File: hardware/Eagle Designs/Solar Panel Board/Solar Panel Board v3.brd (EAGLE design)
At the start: 82.4 x 96.7 mm, 44 parts, among them J1 MOLEX_503763-0291MOLEX_503763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, J2 MOLEX_503763-0491MOLEX_503763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, J3 MOLEX_503763-0291MOLEX_503763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, U1 TMP36GSZ, U2 INA219BIDR

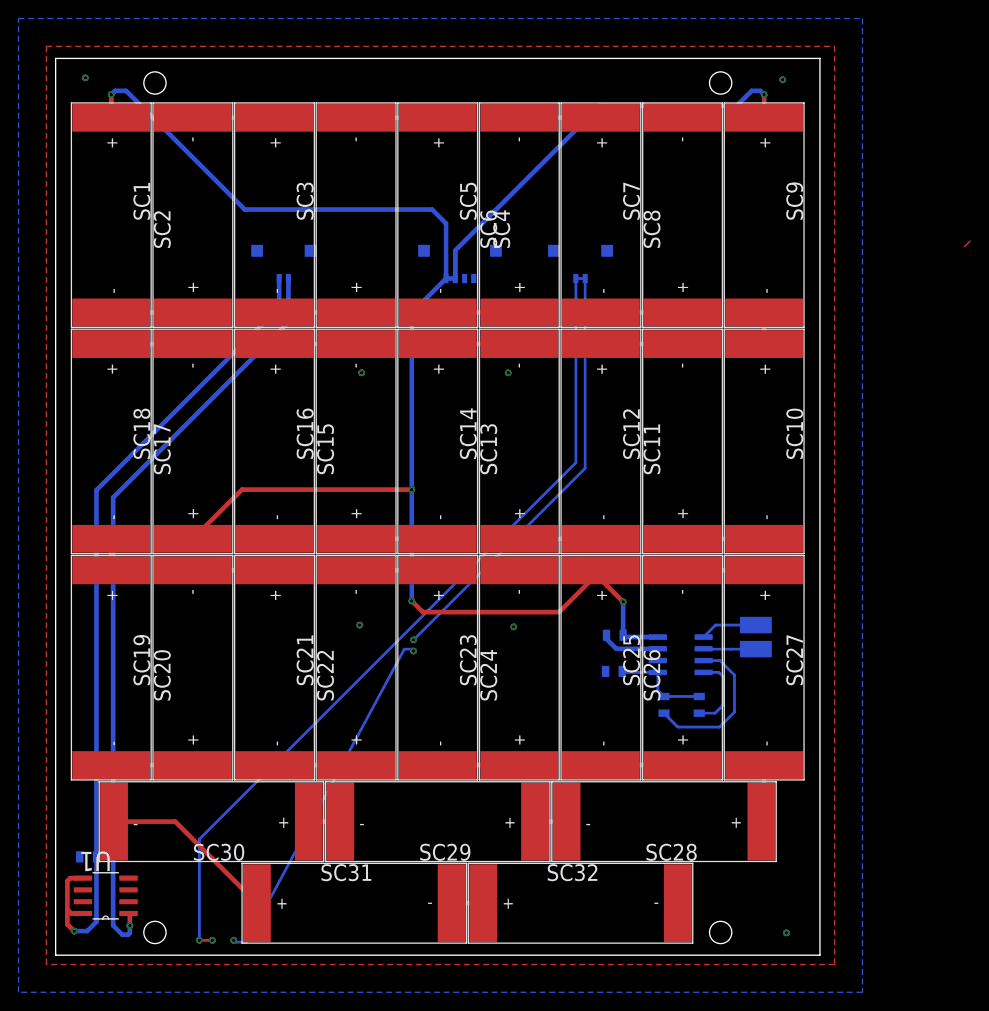
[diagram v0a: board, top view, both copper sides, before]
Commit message: Updated antenna and solar panel boards.
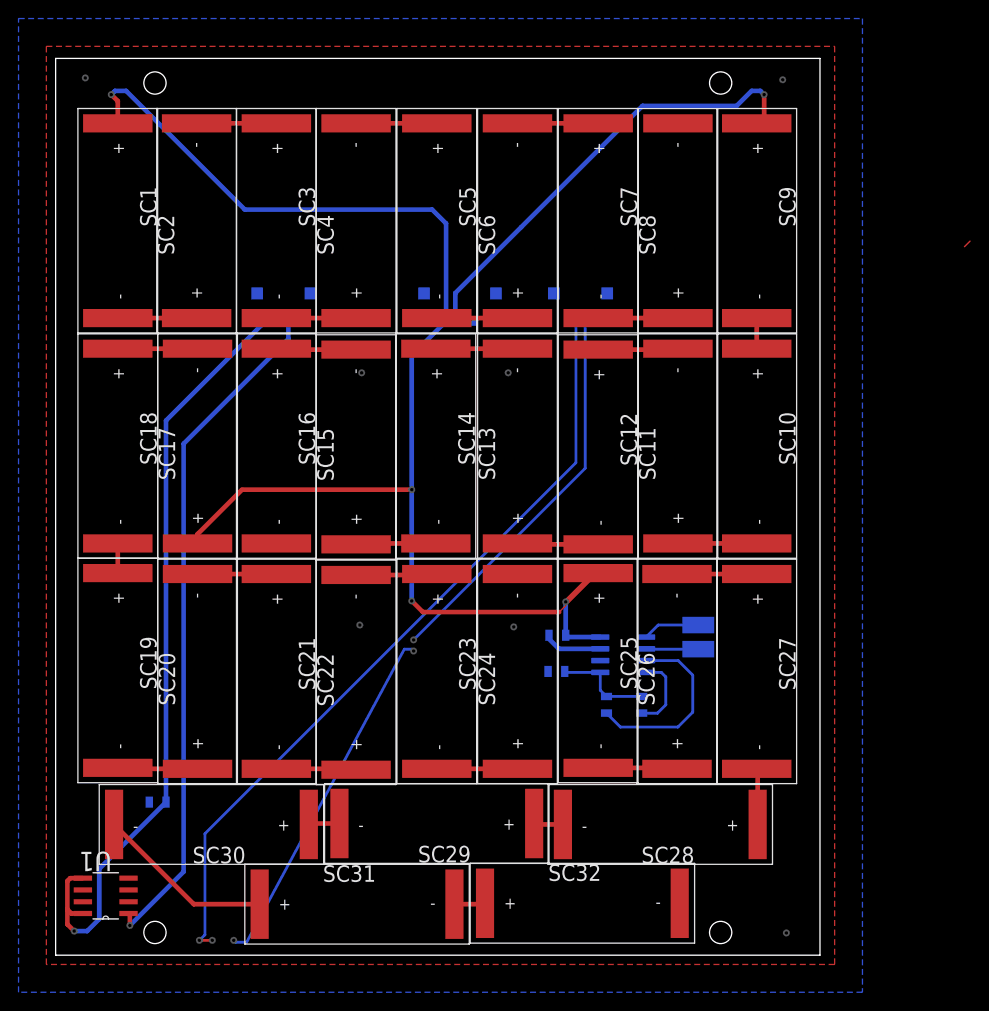
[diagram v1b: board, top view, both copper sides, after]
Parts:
- SC1, SC10, SC11, SC12, SC13, SC14, SC15, SC16, SC17, SC18, SC19, SC2, SC20, SC21, SC22, SC23, SC24, SC25, SC26, SC27, SC28, SC29, SC3, SC30, SC31, SC32, SC4, SC5, SC6, SC7, SC8, SC9: device KXOB25-05X3F:KXOB25-05X3F -> untitled:KXOB25-05X3F
- moved C1 9.54 mm to (11.0, 16.5)
- moved C2 6.20 mm to (54.0, 30.6)
- moved R2 6.20 mm to (63.2, 27.0)
- moved U$1 6.20 mm to (69.3, 33.0)
- moved U$2 6.20 mm to (69.3, 35.6)
- moved U2 6.20 mm to (61.2, 32.4)
- moved R1 6.20 mm to (59.4, 27.0)
- moved R3 6.20 mm to (54.1, 34.5)
- moved J1 4.60 mm to (56.6, 70.8)
- moved J2 4.60 mm to (43.6, 70.8)
- moved J3 4.60 mm to (24.6, 70.8)
- moved SC9 1.00 mm to (75.6, 79.2)
- moved SC10 0.94 mm to (75.6, 54.9)
- moved SC1 0.92 mm to (6.70, 79.2)
- moved SC27 0.89 mm to (75.6, 30.6)
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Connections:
- removed net N$12 (its old number): SC12.-, SC13.+
- removed net N$14 (its old number): SC14.-, SC15.+
- removed net N$19 (its old number): SC20.-, SC21.+
- removed net N$26: SC28.-, SC29.+
- removed net N$28: SC30.-, SC31.+
- removed net N$5 (its old number): SC4.-, SC5.+
- removed net N$7 (its old number): SC6.-, SC7.+
- new net N$15: SC20.-, SC21.+, SC22.-, SC23.+
- new net N$3: SC4.-, SC5.+, SC6.-, SC7.+
- new net N$9: SC12.-, SC13.+, SC14.-, SC15.+
- net N$21: now also SC28.-, SC29.+, SC30.-, SC31.+; no longer SC22.-, SC23.+
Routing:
- net N$28: track 19.0 -> 0.00 mm
- net N$3: track 0.00 -> 18.8 mm
- net N$9: track 0.00 -> 17.4 mm
- net N$15: track 0.00 -> 17.2 mm
- net N$21: track 8.80 -> 22.4 mm
- net N$1: track 22233.0 -> 22223.8 mm
- net N$5 (its old number): track 8.80 -> 0.00 mm
- net N$14 (its old number): track 8.80 -> 0.00 mm
- net N$19 (its old number): track 8.80 -> 0.00 mm
- net N$7 (its old number): track 8.80 -> 0.00 mm
- net N$12 (its old number): track 8.80 -> 0.00 mm
- net VOUT: track 82.0 -> 73.6 mm
- net VCC: track 194.4 -> 198.7 mm
- net VS+: track 89.7 -> 86.0 mm
- net N$36: track 16.9 -> 20.3 mm
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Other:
- outline, holes or cut-outs redrawn

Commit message: Updated antenna and solar panel boards
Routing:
- net VCC: track 198.7 -> 193.7 mm
